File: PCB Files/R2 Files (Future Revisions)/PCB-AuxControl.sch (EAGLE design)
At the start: 16 parts, among them K1 JZC-11F, K2 JZC-11F, T1 NPN2222A, T2 NPN2222A

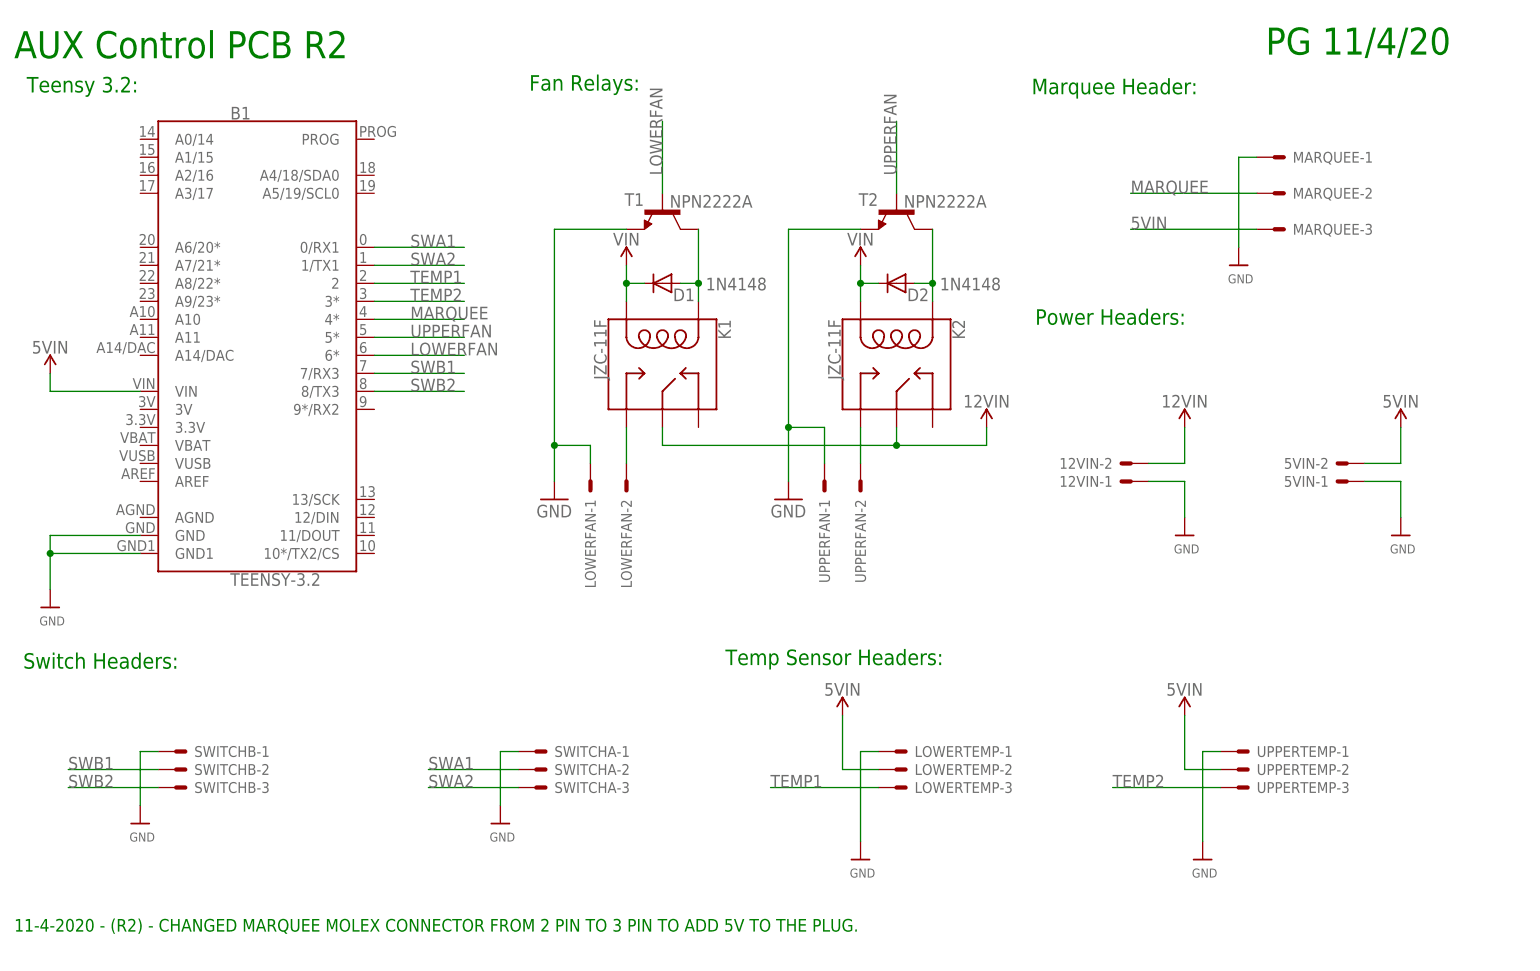
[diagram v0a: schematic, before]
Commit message: AUX Control PCB Update
Added a 4 pin header to the Aux Control PCB to add a remote 2x20 IC Screen for Status/ Cabinet Temp display.
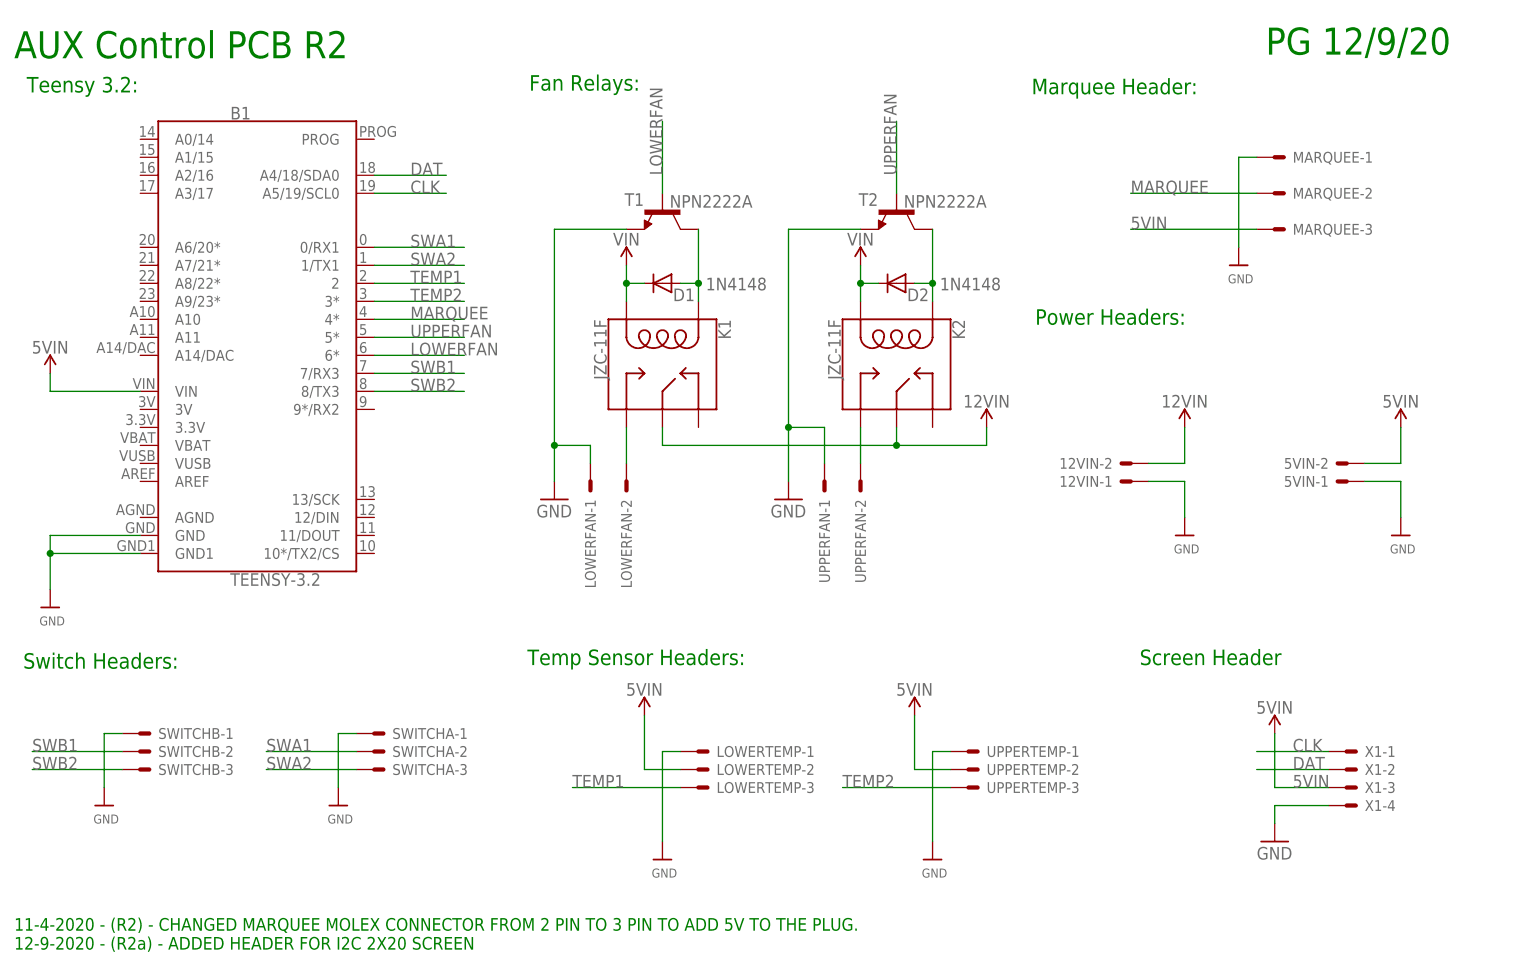
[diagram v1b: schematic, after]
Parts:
- added X1: (no value), con-molex:KK-156-4
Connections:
- new net CLK: B1.A5/19/SCL0, X1-1.S
- new net DAT: B1.A4/18/SDA0, X1-2.S
- net 5VIN: now also X1-3.S
- net GND: now also X1-4.S
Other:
- note added: "11-4-2020 - (R2) - CHANGED MARQUEE MOLEX CONNECTOR FROM 2 PIN TO 3 PIN TO ADD 5V TO THE PLUG. 12-9-2020 - (R2a) - ADDED HEADER FOR I2C 2X20 SCREEN"
- note added: "PG 12/9/20"
- note added: "Screen Header"
- note removed: "11-4-2020 - (R2) - CHANGED MARQUEE MOLEX CONNECTOR FROM 2 PIN TO 3 PIN TO ADD 5V TO THE PLUG."
- note removed: "PG 11/4/20"
- moved on the sheet: LOWERTEMP-1, LOWERTEMP-2, LOWERTEMP-3, SWITCHA-1, SWITCHA-2, SWITCHA-3, SWITCHB-1, SWITCHB-2, SWITCHB-3, UPPERTEMP-1, UPPERTEMP-2, UPPERTEMP-3
